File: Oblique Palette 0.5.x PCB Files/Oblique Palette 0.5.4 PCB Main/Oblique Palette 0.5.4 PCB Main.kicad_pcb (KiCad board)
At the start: 2 copper layers, 235 x 110 mm, 304 parts, among them J1 Conn_01x03_Male_Pin, J10 Conn_01x03_Male_Pin, J12 Conn_01x03_Male_Pin, J15 Conn_01x03_Male_Pin, J16 Conn_01x03_Female_Pin, J17 AudioJack2_SwitchT, J18 Conn_01x03_Male_Pin, J19 Conn_01x03_Female_Pin, J20 AudioJack2_SwitchT, J22 Conn_01x03_Female_Pin, J23 AudioJack2_SwitchT, J25 Conn_01x03_Female_Pin, J26 AudioJack2_SwitchT, J28 Conn_01x03_Female_Pin, J29 AudioJack2_SwitchT, J3 Conn_01x03_Male_Pin, J31 Conn_01x03_Female_Pin, J32 AudioJack2_SwitchT, J34 Conn_01x03_Female_Pin, J35 AudioJack2_SwitchT, J37 Conn_01x03_Female_Pin, J38 AudioJack2_SwitchT, J40 Conn_01x03_Female_Pin, J42 AudioJack2_SwitchT, J44 Conn_01x03_Female_Pin, J46 AudioJack2_SwitchT, J48 Conn_01x03_Female_Pin, J50 AudioJack2_SwitchT, J52 Conn_01x03_Female_Pin, J54 AudioJack2_SwitchT, J56 Conn_01x03_Female_Pin, J58 AudioJack2_SwitchT, J6 Conn_01x03_Male_Pin, J60 Conn_01x03_Female_Pin, J62 AudioJack2_SwitchT, J64 Conn_01x03_Female_Pin, J66 AudioJack2_SwitchT, J68 Conn_01x03_Female_Pin, J70 AudioJack2_SwitchT, J8 Conn_01x03_Male_Pin, U1 CD4051B, U10 MCP6004, U11 MCP4725xxx-xCH, U12 MCP6004, U13 MCP4725xxx-xCH, U14 MCP6004, U15 MCP4725xxx-xCH, U16 MCP6004, U17 MCP4725xxx-xCH, U18 MCP6004, U19 MCP4725xxx-xCH, U2 Pico, U20 MCP6004, U21 MCP4725xxx-xCH, U22 MCP6004, U23 MCP4725xxx-xCH, U24 MCP6004, U25 MCP4725xxx-xCH, U26 MCP6004, U3 MCP6004, U4 MCP6004, U5 MCP6004, U6 MCP6004, U7 MCP6004, U8 MCP6004, U9 MCP6004

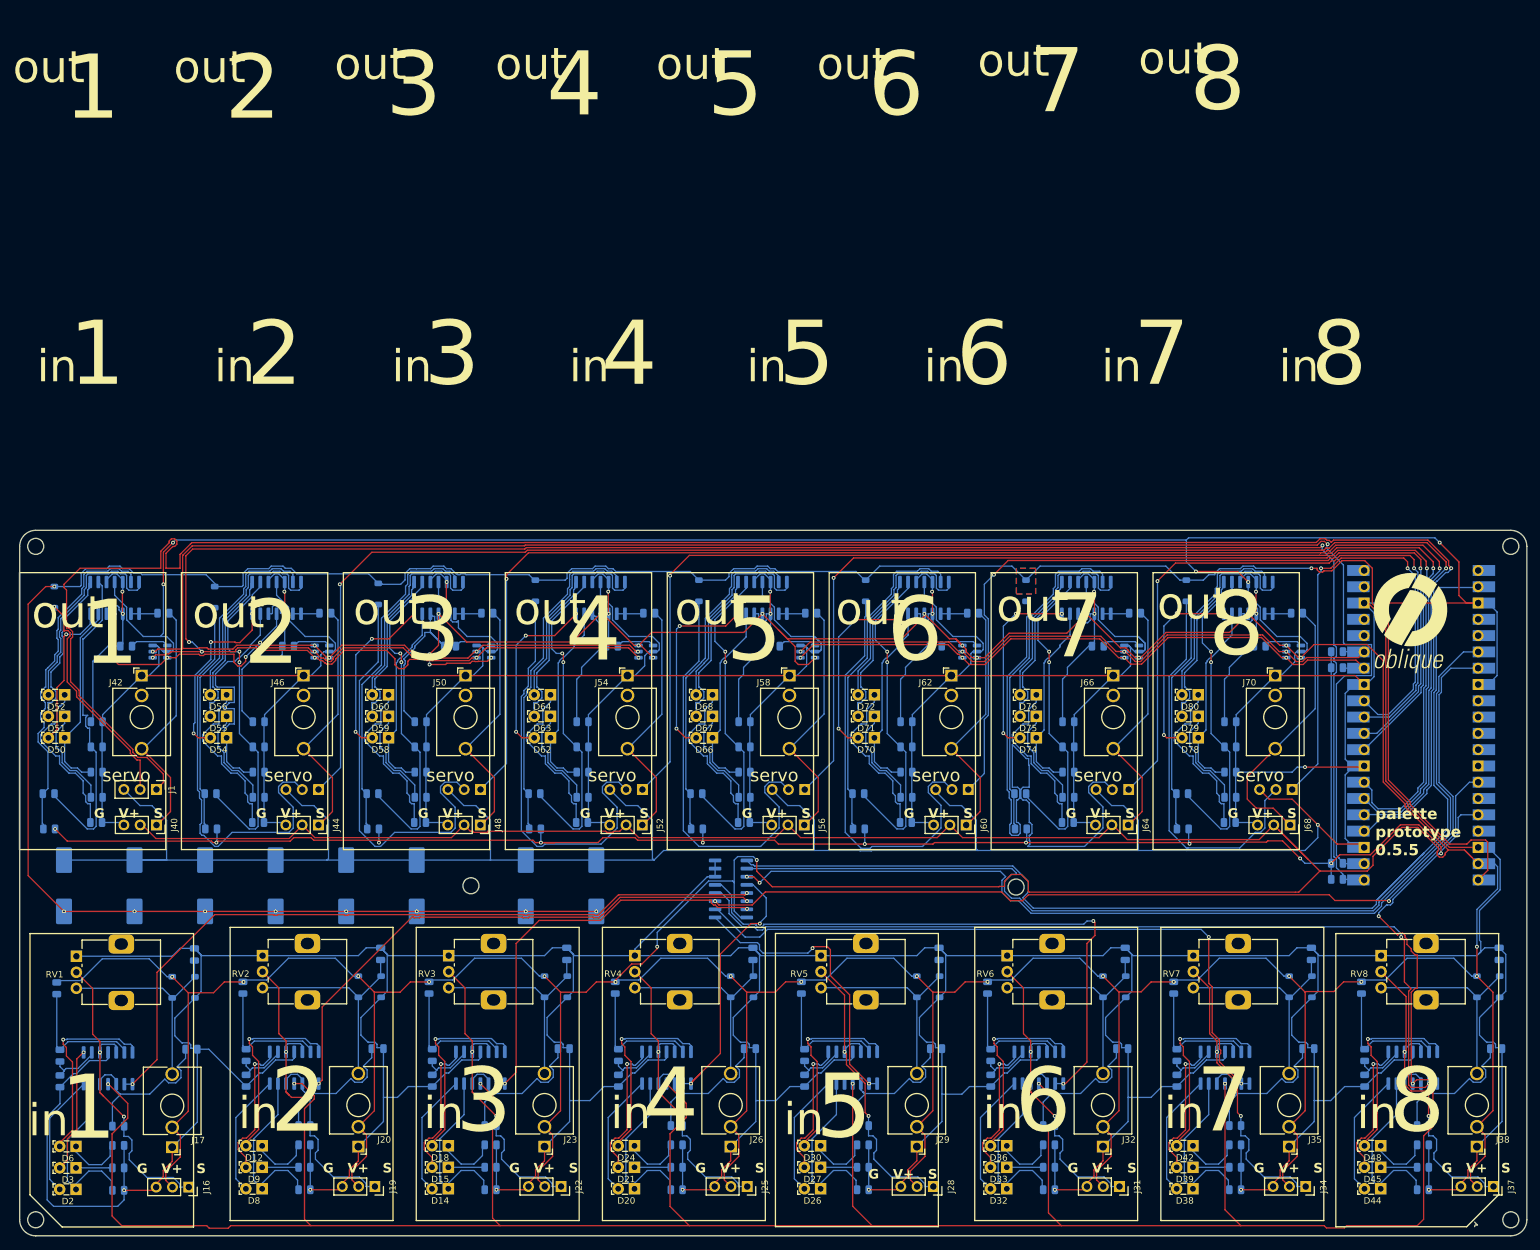
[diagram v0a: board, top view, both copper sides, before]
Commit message: Tidying up just so I can roll back changes to avoid the component re-designation catastrophe.
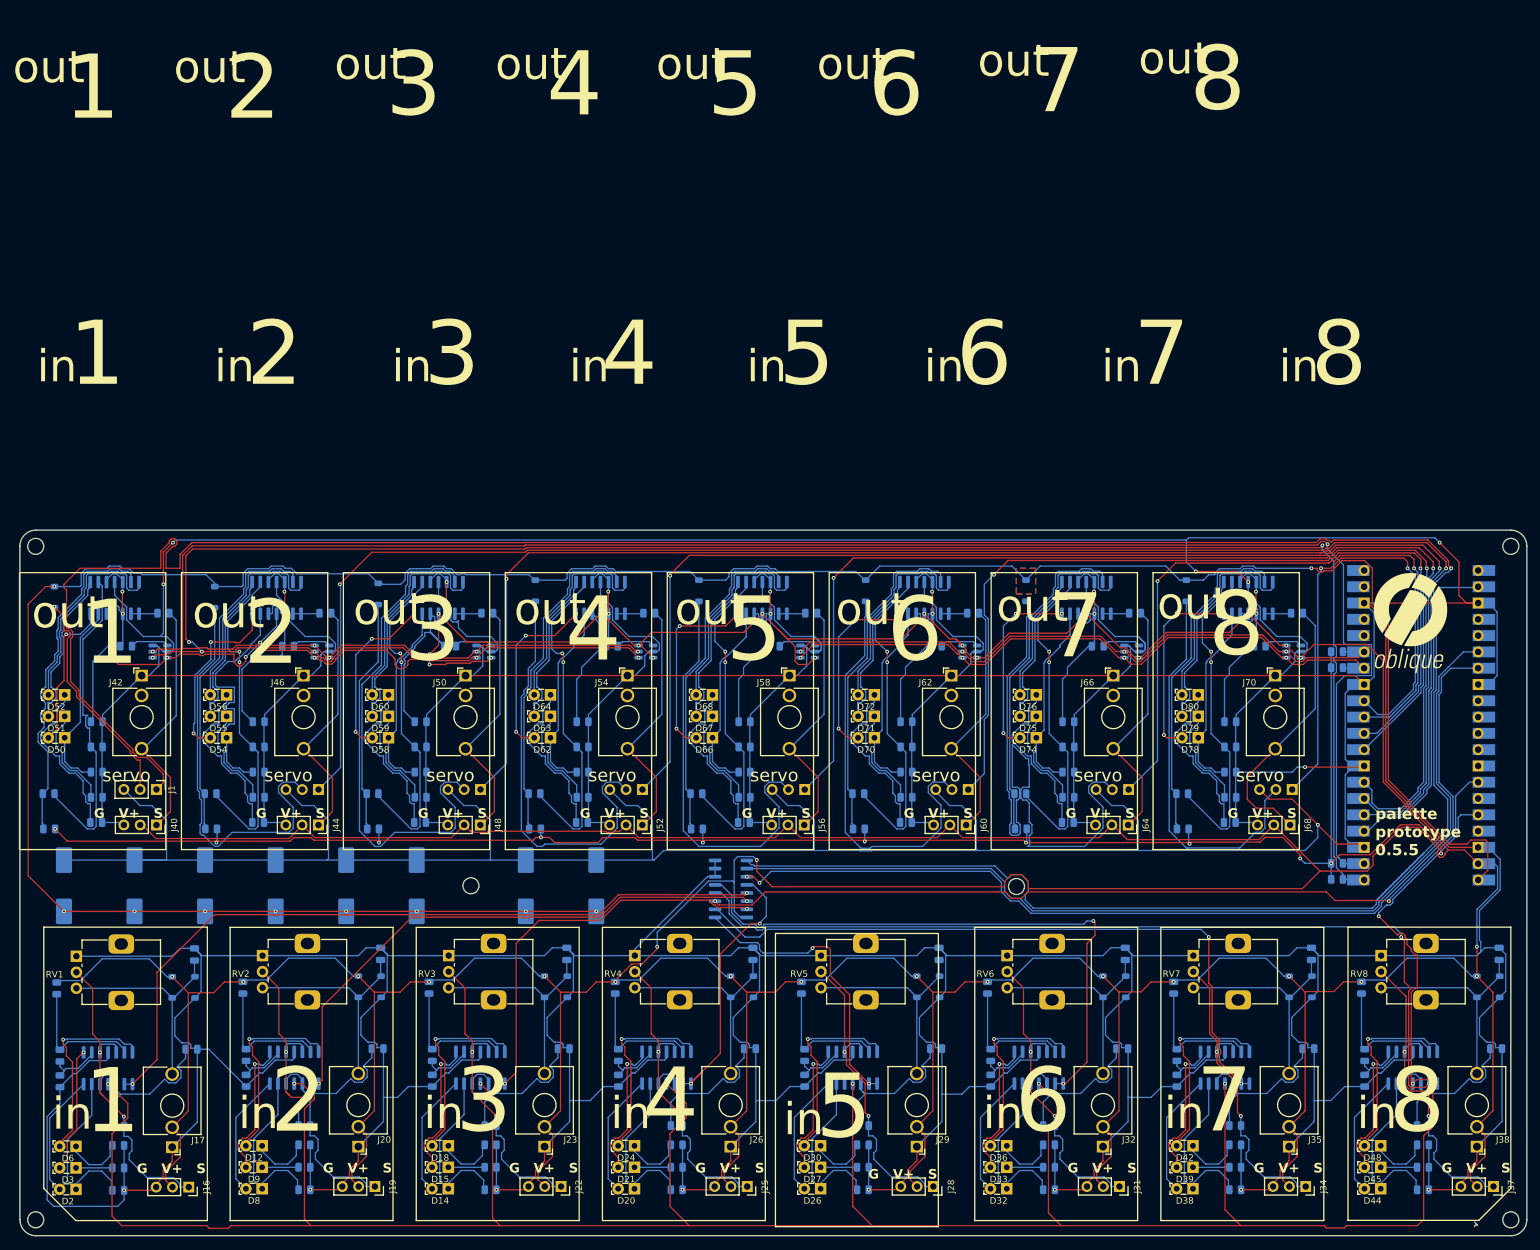
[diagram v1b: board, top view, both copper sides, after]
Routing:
- net VCC: track 1228.8 -> 1220.1 mm
- net Net-(U1-B): track 155.4 -> 151.7 mm
- net GNDREF: track 2224.2 -> 2221.1 mm
- net +3.3V: track 734.6 -> 732.8 mm
- net Net-(U1-A): track 153.2 -> 151.8 mm
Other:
- outline, holes or cut-outs redrawn

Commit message: Fixed that weird component re-designation problem. Everything looks ok now.
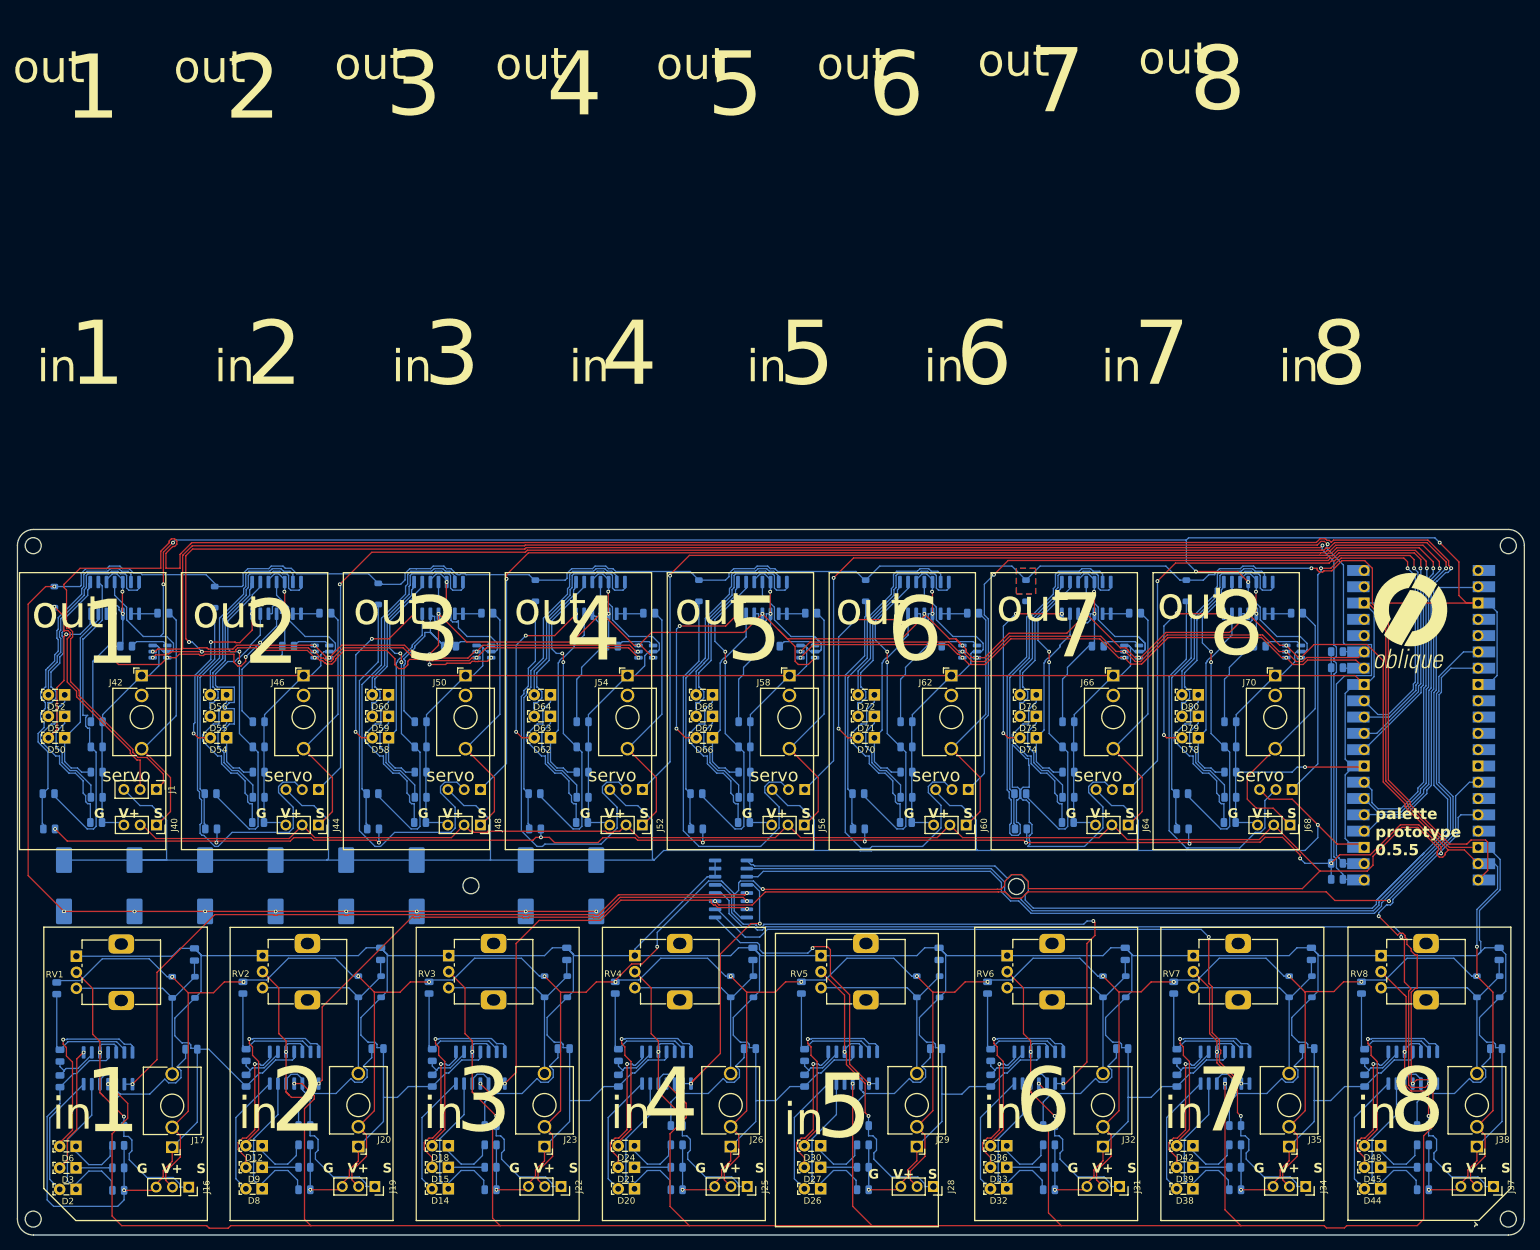
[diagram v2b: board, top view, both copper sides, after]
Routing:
- net VCC: track 1220.1 -> 1215.4 mm
- net /Input 4/ANALOG_CHANNEL: track 42.5 -> 41.6 mm
- net Net-(U1-A): track 151.8 -> 151.0 mm, vias 2 -> 0
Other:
- outline, holes or cut-outs redrawn

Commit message: Penultimate prep for JLCPCB manufacture. Have to place front side still.
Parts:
- removed C17: 1mF, Capacitor_SMD:CP_Elec_10x10
- removed D49: ~, Diode_SMD:D_SOD-123
- added C1: 1mF, Capacitor_SMD:CP_Elec_10x10.5, B.Cu at (106.5, 70.5)
- added D1: ~, Diode_SMD:D_SOD-123, F.Cu at (22.0, 25.4)
- C18, C19, C20, C21, C22, C23, C24: footprint Capacitor_SMD:CP_Elec_10x10 -> Capacitor_SMD:CP_Elec_10x10.5
- J10, J12, J15, J18, J3, J6, J8: moved to F.Cu
- moved G1 2.00 mm to (235.5, 27.2)
- moved G2 2.00 mm to (235.2, 35.2)
- turned J10 to -90 degrees
- turned J12 to -90 degrees
- turned J15 to -90 degrees
- turned J3 to -90 degrees
- turned J6 to -90 degrees
- turned J8 to -90 degrees
- turned J18 to -90 degrees
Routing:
- net GNDREF: track 2221.1 -> 2242.4 mm, vias 16 -> 15
- net VCC: track 1215.4 -> 1231.1 mm, vias 41 -> 40
- net +3.3V: track 732.8 -> 747.6 mm
- net SERVO_1: track 322.5 -> 307.8 mm
- net Net-(U1-C): track 176.6 -> 165.7 mm
- net Net-(U1-X): track 132.7 -> 135.6 mm
- net /Input 8/ANALOG_CHANNEL: track 140.4 -> 138.9 mm
- net Net-(J37-Pin_1): track 50.9 -> 52.2 mm
- net Net-(J40-Pin_1): track 38.5 -> 39.7 mm
- net SERVO_6: track 136.0 -> 135.2 mm
- net SERVO_7: track 106.9 -> 106.2 mm
- net Net-(D1-K): track 35.2 -> 34.5 mm, vias 1 -> 0
- net /Input 1/ANALOG_CHANNEL: track 117.9 -> 118.5 mm
- net SERVO_2: track 258.1 -> 257.5 mm
- net SERVO_4: track 206.1 -> 205.5 mm
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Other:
- outline, holes or cut-outs redrawn
